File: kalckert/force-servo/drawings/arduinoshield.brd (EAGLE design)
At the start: 100 x 80 mm, 24 parts, among them IC1 MCP604P, IC3 7806T

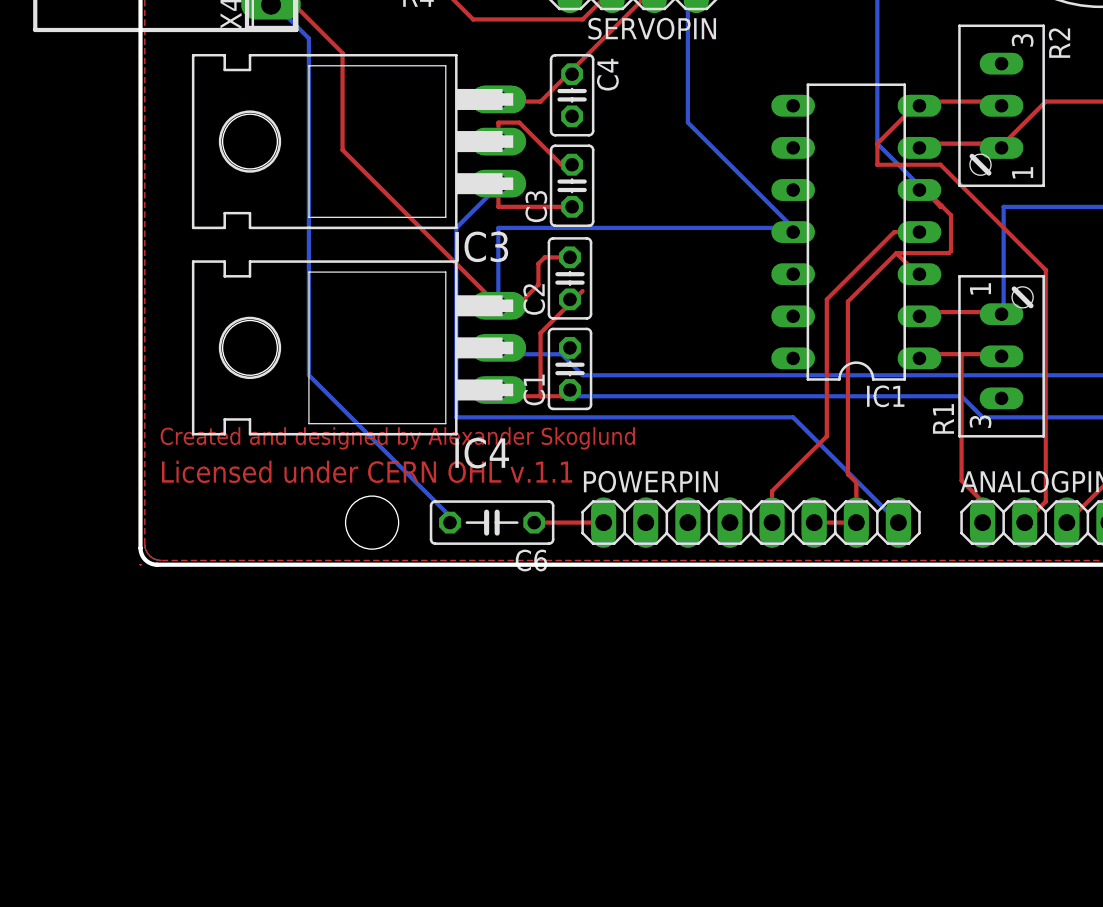
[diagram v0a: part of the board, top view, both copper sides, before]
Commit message: Tuning the PD controller gains, not yet stable. Updated schematic with the LP filter.
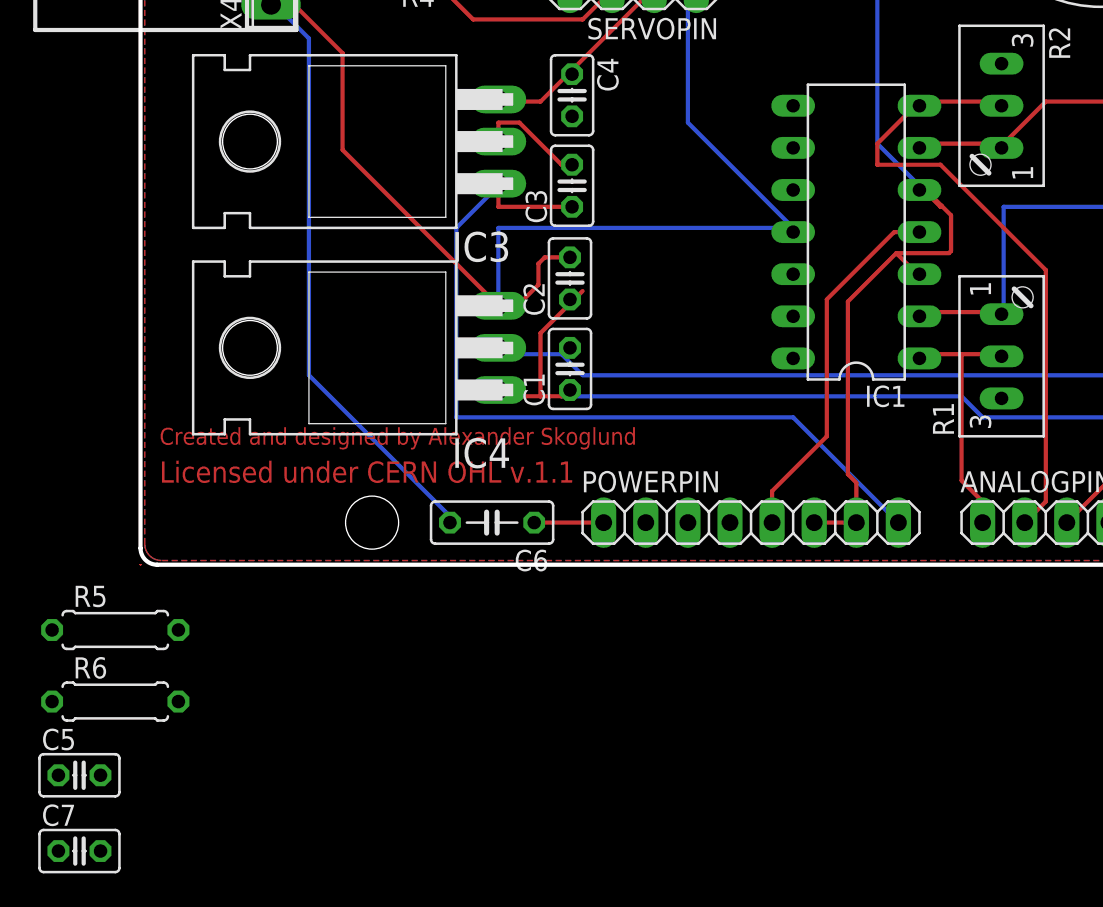
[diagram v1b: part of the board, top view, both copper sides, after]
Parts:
- added C5, C7: 0.1uF, resistor:C025-025X050
- added R5, R6: 82k, resistor:0207/7
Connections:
- new net N$12: IC1.1, R1.S, R5.1
- new net N$13: IC1.7, R2.S, R6.1
- net AMP_FORCE1: now also C5.1, R5.2; no longer IC1.1, R1.S
- net AMP_FORCE2: now also C7.1, R6.2; no longer IC1.7, R2.S
- net GND: now also C5.2, C7.2
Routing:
- net AMP_FORCE2: track 38.7 -> 37.2 mm
- net AMP_FORCE1: track 15.9 -> 14.5 mm
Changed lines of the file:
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@@
 <layers>
 <layer number="1" name="Top" color="4" fill="1" visible="yes" active="yes"/>
-<layer number="16" name="Bottom" color="1" fill="1" visible="no" active="yes"/>
-<layer number="17" name="Pads" color="2" fill="1" visible="no" active="yes"/>
-<layer number="18" name="Vias" color="2" fill="1" visible="no" active="yes"/>
-<layer number="19" name="Unrouted" color="6" fill="1" visible="no" active="yes"/>
-<layer number="20" name="Dimension" color="15" fill="1" visible="no" active="yes"/>
+<layer number="16" name="Bottom" color="1" fill="1" visible="yes" active="yes"/>
+<layer number="17" name="Pads" color="2" fill="1" visible="yes" active="yes"/>
+<layer number="18" name="Vias" color="2" fill="1" visible="yes" active="yes"/>
+<layer number="19" name="Unrouted" color="6" fill="1" visible="yes" active="yes"/>
+<layer number="20" name="Dimension" color="15" fill="1" visible="yes" active="yes"/>
 <layer number="21" name="tPlace" color="7" fill="1" visible="yes" active="yes"/>
 <layer number="22" name="bPlace" color="7" fill="1" visible="no" active="yes"/>
-<layer number="23" name="tOrigins" color="15" fill="1" visible="no" active="yes"/>
-<layer number="24" name="bOrigins" color="15" fill="1" visible="no" active="yes"/>
-<layer number="25" name="tNames" color="7" fill="1" visible="no" active="yes"/>
-<layer number="26" name="bNames" color="7" fill="1" visible="no" active="yes"/>
+<layer number="23" name="tOrigins" color="15" fill="1" visible="yes" active="yes"/>
+<layer number="24" name="bOrigins" color="15" fill="1" visible="yes" active="yes"/>
+<layer number="25" name="tNames" color="7" fill="1" visible="yes" active="yes"/>
+<layer number="26" name="bNames" color="7" fill="1" visible="yes" active="yes"/>
 <layer number="27" name="tValues" color="7" fill="1" visible="no" active="yes"/>
 <layer number="28" name="bValues" color="7" fill="1" visible="no" active="yes"/>
@@
 </element>
 <element name="C6" library="resistor" package="C050-025X075" value="10uF" x="21.209" y="2.54" rot="R180"/>
+<element name="R5" library="resistor" package="0207/7" value="82k" x="-1.524" y="-3.937"/>
+<element name="R6" library="resistor" package="0207/7" value="82k" x="-1.524" y="-8.255"/>
+<element name="C5" library="resistor" package="C025-025X050" value="0.1uF" x="-3.683" y="-12.7"/>
+<element name="C7" library="resistor" package="C025-025X050" value="0.1uF" x="-3.683" y="-17.272"/>
 </elements>
 <signals>
@@
 <wire x1="19.05" y1="2.54" x2="18.669" y2="2.54" width="0.254" layer="16"/>
 <wire x1="8.89" y1="33.02" x2="7.874" y2="33.782" width="0.254" layer="16"/>
+<contactref element="C7" pad="2"/>
+<contactref element="C5" pad="2"/>
+<wire x1="-2.413" y1="-12.7" x2="18.669" y2="2.54" width="0" layer="19" extent="1-1"/>
+<wire x1="-2.413" y1="-17.272" x2="-2.413" y2="-12.7" width="0" layer="19" extent="1-1"/>
 </signal>
 <signal name="VCCSERVO">
@@
 </signal>
 <signal name="AMP_FORCE1">
-<contactref element="IC1" pad="1"/>
-<contactref element="R1" pad="S"/>
 <contactref element="ANALOGPIN" pad="1"/>
 <wire x1="50.8" y1="12.7" x2="49.53" y2="12.7" width="0.254" layer="1"/>
 <wire x1="49.53" y1="12.7" x2="46.99" y2="12.7" width="0.254" layer="1"/>
-<wire x1="46.99" y1="12.7" x2="46.99" y2="12.446" width="0.254" layer="1"/>
-<wire x1="50.8" y1="12.7" x2="51.943" y2="12.573" width="0.254" layer="1"/>
 <wire x1="49.53" y1="5.08" x2="50.8" y2="3.81" width="0.254" layer="1"/>
 <wire x1="49.53" y1="12.7" x2="49.53" y2="5.08" width="0.254" layer="1"/>
 <wire x1="50.8" y1="3.81" x2="50.8" y2="2.54" width="0.254" layer="1"/>
+<contactref element="R5" pad="2"/>
+<contactref element="C5" pad="1"/>
+<wire x1="2.286" y1="-3.937" x2="46.99" y2="12.7" width="0" layer="19" extent="1-1"/>
+<wire x1="-4.953" y1="-12.7" x2="2.286" y2="-3.937" width="0" layer="19" extent="1-1"/>
 </signal>
 <signal name="AMP_FORCE2">
-<contactref element="R2" pad="S"/>
-<contactref element="IC1" pad="7"/>
 <contactref element="ANALOGPIN" pad="2"/>
 <wire x1="50.8" y1="27.94" x2="46.99" y2="27.94" width="0.254" layer="1"/>
-<wire x1="50.8" y1="27.94" x2="51.943" y2="27.686" width="0.254" layer="1"/>
 <wire x1="54.61" y1="3.81" x2="53.34" y2="2.54" width="0.254" layer="1"/>
 <wire x1="54.61" y1="17.78" x2="54.61" y2="3.81" width="0.254" layer="1"/>
@@
 <wire x1="44.45" y1="25.4" x2="44.45" y2="24.13" width="0.254" layer="1"/>
 <wire x1="46.99" y1="27.94" x2="44.45" y2="25.4" width="0.254" layer="1"/>
-<wire x1="46.99" y1="27.94" x2="46.99" y2="27.686" width="0.254" layer="1"/>
+<contactref element="R6" pad="2"/>
+<contactref element="C7" pad="1"/>
+<wire x1="2.286" y1="-8.255" x2="53.34" y2="2.54" width="0" layer="19" extent="1-1"/>
+<wire x1="-4.953" y1="-17.272" x2="2.286" y2="-8.255" width="0" layer="19" extent="1-1"/>
 </signal>
 <signal name="SLIDER_POT">
@@
 <wire x1="0.000378125" y1="-0.000915625" x2="0.000834375" y2="-0.00201875" width="0.000253125" layer="1"/>
 </signal>
+<signal name="N$12">
+<contactref element="IC1" pad="1"/>
+<contactref element="R5" pad="1"/>
+<contactref element="R1" pad="S"/>
+<wire x1="46.99" y1="12.446" x2="51.943" y2="12.573" width="0" layer="19" extent="1-1"/>
+<wire x1="-5.334" y1="-3.937" x2="46.99" y2="12.446" width="0" layer="19" extent="1-1"/>
+</signal>
+<signal name="N$13">
+<contactref element="R2" pad="S"/>
+<contactref element="R6" pad="1"/>
+<contactref element="IC1" pad="7"/>
+<wire x1="46.99" y1="27.686" x2="51.943" y2="27.686" width="0" layer="19" extent="1-1"/>
+<wire x1="-5.334" y1="-8.255" x2="46.99" y2="27.686" width="0" layer="19" extent="1-1"/>
+</signal>
 </signals>

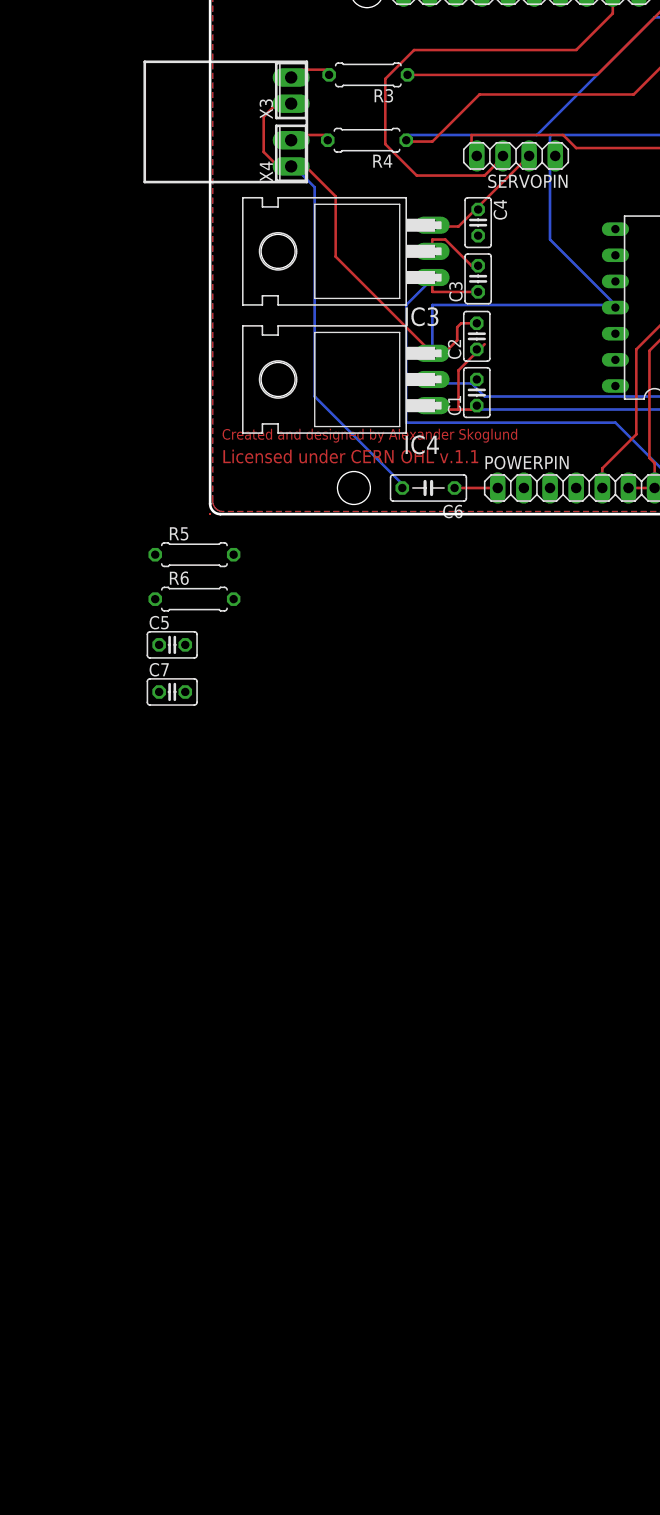
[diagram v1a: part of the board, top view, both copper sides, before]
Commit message: Updated power regulator
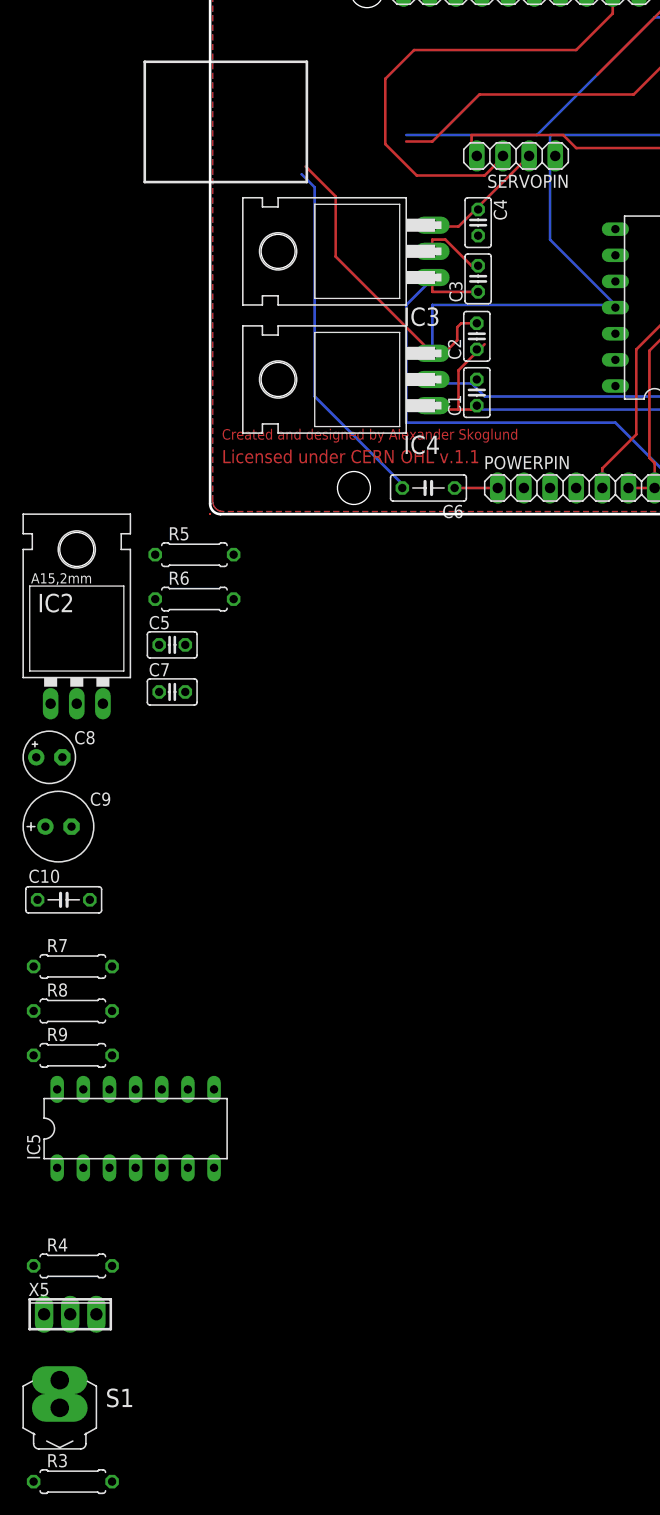
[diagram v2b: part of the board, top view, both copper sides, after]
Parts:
- removed X3, X4: (no value), con-phoenix-254:2POL254
- added C10: 0.1uF, resistor:C050-025X075
- added C8: 10uF, resistor:E2,5-5
- added C9: 100uF, resistor:E2,5-7
- added IC2: (no value), v-reg:317TL
- added IC5: MCP604P, linear:DIL14
- added R7: 220, resistor:0207/7
- added R8: 560, resistor:0207/7
- added R9: 270, resistor:0207/7
- added S1: (no value), switch:MS243
- added X5: (no value), con-phoenix-254:3POL254
- R3: value 10k -> 68
- R4: value 10k -> 82k
- moved R3 139.6 mm to (-13.3, -94.0), turned to 0 degrees
- moved R4 113.0 mm to (-13.3, -73.0), turned to 0 degrees
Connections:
- new net N$14: C9.+, IC2.3
- new net N$19: R8.1, R9.2, S1.1
- new net N$20: C10.1, C8.+, IC2.2, R7.2
- new net N$23: IC2.1, R7.1, R8.2
- new net N$5: IC5.1, IC5.4
- new net V-: IC5.11
- net GND: now also C10.2, C8.-, C9.-, R3.1, R4.1, R9.1; no longer X3.1, X4.1
- net LED_GREEN: now also DIGITALPIN0-7.1, X5.1; no longer R3.2, X3.2
- net LED_RED: now also DIGITALPIN0-7.2, X5.2; no longer R4.2, X4.2
- net N$1: now also R4.2; no longer DIGITALPIN0-7.1, R3.1
- net N$4: now also R3.2, S1.2; no longer DIGITALPIN0-7.2, R4.1
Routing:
- net N$4: track 74.0 -> 0.00 mm
- net LED_RED: track 4.18 -> 73.5 mm
- net N$1: track 29.9 -> 0.00 mm
- net GND: track 193.0 -> 180.5 mm
- net LED_GREEN: track 4.33 -> 11.5 mm
